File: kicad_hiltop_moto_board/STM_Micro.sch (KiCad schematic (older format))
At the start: 19 parts, among them SW1 SW_Push, U22 STM32F072RBTx, Y2 8MHZ, Y3 ABS25-32.768KHZ-6-T

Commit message: Unused pind removed from moto board
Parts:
- C73, C74, C75, C76, C77, C78, C79, C80, C81, C82: symbol Motor_Control_Board-rescue:C-device-Sensi_Board-rescue -> moto_board-rescue:C-device-Sensi_Board-rescue-Motor_Control_Board-rescue
- D13: symbol Motor_Control_Board-rescue:LED-device-Sensi_Board-rescue -> moto_board-rescue:LED-device-Sensi_Board-rescue-Motor_Control_Board-rescue
- L11: symbol Motor_Control_Board-rescue:Ferrite_Bead-device-Sensi_Board-rescue -> moto_board-rescue:Ferrite_Bead-device-Sensi_Board-rescue-Motor_Control_Board-rescue
- R120, R124: symbol Motor_Control_Board-rescue:R-device-Sensi_Board-rescue -> moto_board-rescue:R-device-Sensi_Board-rescue-Motor_Control_Board-rescue
- TP126: symbol Motor_Control_Board-rescue:Test_Point-Connector-Sensi_Board-rescue -> moto_board-rescue:Test_Point-Connector-Sensi_Board-rescue-Motor_Control_Board-rescue
- U22: symbol Motor_Control_Board-rescue:STM32F072RBTx-MCU_ST_STM32-Sensi_Board-rescue -> moto_board-rescue:STM32F072RBTx-MCU_ST_STM32-Sensi_Board-rescue-Motor_Control_Board-rescue
- Y2: symbol Motor_Control_Board-rescue:Crystal_GND24-device-Sensi_Board-rescue -> moto_board-rescue:Crystal_GND24-device-Sensi_Board-rescue-Motor_Control_Board-rescue
- Y3: symbol Motor_Control_Board-rescue:Crystal_GND23-device-Sensi_Board-rescue -> moto_board-rescue:Crystal_GND23-device-Sensi_Board-rescue-Motor_Control_Board-rescue
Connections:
- net labels added: STM_RES1, STM_RES2
- net labels removed: ADC1, ADC10, ADC11, ADC12, ADC13, ADC2, ADC3, ADC4, ADC5, ADC6, ADC7, ADC8, ADC9, GPIO10, GPIO11, GPIO12, GPIO13, GPIO14, GPIO15, GPIO16, GPIO17, GPIO18, GPIO19, GPIO9, STM_SCL, STM_SDA
- wire segments 131 -> 124
- no-connect marks 6 -> 30
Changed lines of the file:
@@
 EESchema Schematic File Version 4
-LIBS:Motor_Control_Board-cache
+LIBS:moto_board-cache
 EELAYER 30 0
 EELAYER END
@@
 $EndDescr
 $Comp
-L Motor_Control_Board-rescue:STM32F072RBTx-MCU_ST_STM32-Sensi_Board-rescue U22
+L moto_board-rescue:STM32F072RBTx-MCU_ST_STM32-Sensi_Board-rescue-Motor_Control_Board-rescue U22
 U 1 1 5F956EB6
 P 7400 4675
@@
 $EndComp
 $Comp
-L Motor_Control_Board-rescue:Ferrite_Bead-device-Sensi_Board-rescue L11
+L moto_board-rescue:Ferrite_Bead-device-Sensi_Board-rescue-Motor_Control_Board-rescue L11
 U 1 1 5F957109
 P 8225 2025
@@
 	8525 2025 8375 2025
 $Comp
-L Motor_Control_Board-rescue:C-device-Sensi_Board-rescue C82
+L moto_board-rescue:C-device-Sensi_Board-rescue-Motor_Control_Board-rescue C82
 U 1 1 5F957430
 P 7875 2250
@@
 $EndComp
 $Comp
-L Motor_Control_Board-rescue:C-device-Sensi_Board-rescue C73
+L moto_board-rescue:C-device-Sensi_Board-rescue-Motor_Control_Board-rescue C73
 U 1 1 5F957A1A
 P 2125 1625
@@
 $EndComp
 $Comp
-L Motor_Control_Board-rescue:C-device-Sensi_Board-rescue C74
+L moto_board-rescue:C-device-Sensi_Board-rescue-Motor_Control_Board-rescue C74
 U 1 1 5F957BC6
 P 2575 1625
@@
 $EndComp
 $Comp
-L Motor_Control_Board-rescue:C-device-Sensi_Board-rescue C79
+L moto_board-rescue:C-device-Sensi_Board-rescue-Motor_Control_Board-rescue C79
 U 1 1 5F957C44
 P 3025 1625
@@
 $EndComp
 $Comp
-L Motor_Control_Board-rescue:C-device-Sensi_Board-rescue C80
+L moto_board-rescue:C-device-Sensi_Board-rescue-Motor_Control_Board-rescue C80
 U 1 1 5F957C84
 P 3475 1625
@@
 	4400 3075 3825 3075
 $Comp
-L Motor_Control_Board-rescue:R-device-Sensi_Board-rescue R120
+L moto_board-rescue:R-device-Sensi_Board-rescue-Motor_Control_Board-rescue R120
 U 1 1 5F95CC59
 P 2725 2850
@@
 BOOT0
 $Comp
-L Motor_Control_Board-rescue:C-device-Sensi_Board-rescue C81
+L moto_board-rescue:C-device-Sensi_Board-rescue-Motor_Control_Board-rescue C81
 U 1 1 5F9616D2
 P 3825 3550
@@
 $EndComp
 $Comp
-L Motor_Control_Board-rescue:Crystal_GND23-device-Sensi_Board-rescue Y3
+L moto_board-rescue:Crystal_GND23-device-Sensi_Board-rescue-Motor_Control_Board-rescue Y3
 U 1 1 5F964614
 P 3225 6550
@@
 	3575 6525 4100 6525
 $Comp
-L Motor_Control_Board-rescue:C-device-Sensi_Board-rescue C77
+L moto_board-rescue:C-device-Sensi_Board-rescue-Motor_Control_Board-rescue C77
 U 1 1 5F96D367
 P 2850 6275
@@
 Connection ~ 3225 6275
 $Comp
-L Motor_Control_Board-rescue:C-device-Sensi_Board-rescue C78
+L moto_board-rescue:C-device-Sensi_Board-rescue-Motor_Control_Board-rescue C78
 U 1 1 5F96FC00
 P 2850 6825
@@
 Connection ~ 3225 6825
 $Comp
-L Motor_Control_Board-rescue:Crystal_GND24-device-Sensi_Board-rescue Y2
+L moto_board-rescue:Crystal_GND24-device-Sensi_Board-rescue-Motor_Control_Board-rescue Y2
 U 1 1 5F97410A
 P 3050 4325
@@
 	3050 4075 3050 4175
 $Comp
-L Motor_Control_Board-rescue:C-device-Sensi_Board-rescue C75
+L moto_board-rescue:C-device-Sensi_Board-rescue-Motor_Control_Board-rescue C75
 U 1 1 5F97DA85
 P 2825 4075
@@
 	2550 4075 2675 4075
 $Comp
-L Motor_Control_Board-rescue:C-device-Sensi_Board-rescue C76
+L moto_board-rescue:C-device-Sensi_Board-rescue-Motor_Control_Board-rescue C76
 U 1 1 5F97DA93
 P 2825 4625
@@
 	10400 4775 11800 4775
 Wire Wire Line
-	4400 4775 3925 4775
-Wire Wire Line
-	4400 4875 3925 4875
-Wire Wire Line
-	4400 5175 3925 5175
-Wire Wire Line
-	4400 5275 3925 5275
-Wire Wire Line
 	3225 6275 4000 6275
 Wire Wire Line
@@
 	10400 3675 11800 3675
 Wire Wire Line
-	4400 5075 3925 5075
-Wire Wire Line
 	10400 4575 11800 4575
 Wire Wire Line
@@
 	10400 5175 11800 5175
 Wire Wire Line
-	4400 4575 3925 4575
-Wire Wire Line
 	10400 6075 11775 6075
 Wire Wire Line
@@
 Wire Wire Line
 	10400 4275 11800 4275
-Wire Wire Line
-	4400 4975 3925 4975
 Wire Wire Line
 	10400 5675 11775 5675
@@
 Text HLabel 11775 5775 2    60   Output ~ 0
 DEBUG_UART_TX
-Text HLabel 11800 3375 2    60   Input ~ 0
-ADC3
-$Comp
-L Motor_Control_Board-rescue:R-device-Sensi_Board-rescue R124
+$Comp
+L moto_board-rescue:R-device-Sensi_Board-rescue-Motor_Control_Board-rescue R124
 U 1 1 5CB16726
 P 12600 3575
@@
 $EndComp
 $Comp
-L Motor_Control_Board-rescue:LED-device-Sensi_Board-rescue D13
+L moto_board-rescue:LED-device-Sensi_Board-rescue-Motor_Control_Board-rescue D13
 U 1 1 5CB1BE49
 P 13075 3575
@@
 Text HLabel 11800 3875 2    60   BiDi ~ 0
 GPIO2
-Text HLabel 11800 4775 2    60   BiDi ~ 0
-GPIO13
-Text HLabel 11775 5575 2    60   BiDi ~ 0
-GPIO10
 Text HLabel 11775 6075 2    60   BiDi ~ 0
 GPIO5
-Text HLabel 3925 4575 0    60   BiDi ~ 0
-GPIO9
-Text HLabel 4400 6075 0    60   BiDi ~ 0
-GPIO11
-Text HLabel 11800 4975 2    60   BiDi ~ 0
-GPIO14
 Text HLabel 11775 6275 2    60   BiDi ~ 0
 GPIO7
-Text HLabel 3925 5175 0    60   Input ~ 0
-ADC12
-Text HLabel 3925 5275 0    60   Input ~ 0
-ADC13
-Text HLabel 11800 3175 2    60   BiDi ~ 0
-GPIO12
 Text HLabel 3925 5575 0    60   BiDi ~ 0
 GPIO1
@@
 	3925 5475 4400 5475
 $Comp
-L Motor_Control_Board-rescue:Test_Point-Connector-Sensi_Board-rescue TP?
+L moto_board-rescue:Test_Point-Connector-Sensi_Board-rescue-Motor_Control_Board-rescue TP?
 U 1 1 62481FA3
 P 7100 1825
@@
 Text HLabel 11800 5275 2    60   Input ~ 0
 STM_SPI1_MOSI
-Text HLabel 11800 5375 2    60   Input ~ 0
-STM_SCL
-Text HLabel 11800 5475 2    60   Input ~ 0
-STM_SDA
 NoConn ~ 4400 5375
 NoConn ~ 4400 3475
@@
 Text HLabel 11800 4475 2    60   Input ~ 0
 SWD_SCK
-Text HLabel 3925 4875 0    60   Input ~ 0
-ADC9
-Text HLabel 3925 4775 0    60   Input ~ 0
-ADC8
-Text HLabel 11800 3475 2    60   Input ~ 0
-ADC4
-Text HLabel 11800 3275 2    60   Input ~ 0
-ADC2
-Text HLabel 11800 3075 2    60   Input ~ 0
-ADC1
 Text HLabel 4400 5675 0    60   BiDi ~ 0
 GPIO3
@@
 Wire Wire Line
 	10400 5975 11800 5975
-Text HLabel 3925 4975 0    60   Input ~ 0
-ADC10
-Text HLabel 3925 5075 0    60   Input ~ 0
-ADC11
 Wire Wire Line
 	7500 1725 7500 1825
-Text HLabel 11800 3675 2    60   Input ~ 0
-ADC5
-Text HLabel 11800 3775 2    60   Input ~ 0
-ADC6
-Text HLabel 11775 4875 2    60   Input ~ 0
-ADC7
 $Comp
 L power:PWR_FLAG #FLG0102
@@
 NoConn ~ 4400 5775
 NoConn ~ 4400 5875
-Text HLabel 4400 5975 0    60   BiDi ~ 0
-GPIO15
-Text HLabel 11800 4075 2    60   BiDi ~ 0
-GPIO16
-Text HLabel 11800 4575 2    60   BiDi ~ 0
-GPIO17
-Text HLabel 11775 5675 2    60   BiDi ~ 0
-GPIO18
-Text HLabel 11800 5975 2    60   BiDi ~ 0
-GPIO19
+NoConn ~ 4400 4575
+NoConn ~ 4400 4775
+NoConn ~ 4400 4875
+NoConn ~ 4400 4975
+NoConn ~ 4400 5075
+NoConn ~ 4400 5175
+NoConn ~ 4400 5275
+NoConn ~ 4400 5975
+NoConn ~ 4400 6075
+NoConn ~ 11800 3075
+NoConn ~ 11800 3175
+NoConn ~ 11800 3275
+NoConn ~ 11800 3375
+NoConn ~ 11800 3475
+NoConn ~ 11800 3675
+NoConn ~ 11800 3775
+NoConn ~ 11800 4075
+NoConn ~ 11800 4575
+NoConn ~ 11800 4875
+NoConn ~ 11800 5375
+NoConn ~ 11800 5475
+NoConn ~ 11775 5575
+NoConn ~ 11775 5675
+NoConn ~ 11800 5975
+Text HLabel 11800 4975 2    60   Input ~ 0
+STM_RES2
+Text HLabel 11800 4775 2    60   Input ~ 0
+STM_RES1
 $EndSCHEMATC

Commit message: Started on moto board layout
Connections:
- net GPIO1 renamed M_SCS
- net GPIO2 renamed M_AIN1
- net GPIO3 renamed M_AIN2
- net GPIO4 renamed M_BIN1
- net GPIO5 renamed M_BIN2
- net GPIO6 renamed M_SLEEPn
- net GPIO7 renamed M_RESET
- net GPIO8 renamed M_FAULTn
- net STM_SPI1_MISO renamed M_SDATO
- net STM_SPI1_MOSI renamed M_SDATI
- net STM_SPI1_SCK renamed M_SCLK
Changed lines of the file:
@@
 $Descr A3 16535 11693
 encoding utf-8
-Sheet 3 5
+Sheet 5 5
 Title ""
 Date "2019-10-01"
@@
 	13325 3575 13225 3575
 Text HLabel 11800 3975 2    60   BiDi ~ 0
-GPIO4
+M_BIN1
 Text HLabel 11800 4175 2    60   Output ~ 0
 USB_DATA_N
@@
 USB_DATA_P
 Text HLabel 11800 3875 2    60   BiDi ~ 0
-GPIO2
+M_AIN1
 Text HLabel 11775 6075 2    60   BiDi ~ 0
-GPIO5
+M_BIN2
 Text HLabel 11775 6275 2    60   BiDi ~ 0
-GPIO7
-Text HLabel 3925 5575 0    60   BiDi ~ 0
-GPIO1
+M_RESET
 Wire Wire Line
 	10400 5075 11800 5075
@@
 	10400 3175 11800 3175
 Text HLabel 3925 5475 0    60   BiDi ~ 0
-GPIO8
+M_FAULTn
 Wire Wire Line
 	2125 3275 4400 3275
 Text HLabel 11800 5075 2    60   Input ~ 0
-STM_SPI1_SCK
+M_SCLK
 Text HLabel 11800 5175 2    60   Input ~ 0
-STM_SPI1_MISO
+M_SDATO
 Text HLabel 11800 5275 2    60   Input ~ 0
-STM_SPI1_MOSI
+M_SDATI
 NoConn ~ 4400 5375
 NoConn ~ 4400 3475
@@
 SWD_SCK
 Text HLabel 4400 5675 0    60   BiDi ~ 0
-GPIO3
+M_AIN2
 Text HLabel 11775 6175 2    60   BiDi ~ 0
-GPIO6
+M_SLEEPn
 Text HLabel 11775 5875 2    60   Input ~ 0
 DEBUG_UART_RX
@@
 Text HLabel 11800 4775 2    60   Input ~ 0
 STM_RES1
+Text HLabel 3925 5575 0    60   BiDi ~ 0
+M_SCS
 $EndSCHEMATC

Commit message: Moto board awaiting review
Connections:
- net M_FAULTn: now also U22.53 (PC12/USART3_CK/USART4_CK); no longer U22.38 (PC7/TIM3_CH2)
- net M_RESET: now also U22.10 (PC2/ADC_IN12/I2S2_MCK/SPI2_MISO); no longer U22.36 (I2S2_SD/RTC_REFIN/SPI2_MOSI/SYS_WKUP7/TIM15_CH1N/TIM15_CH2/TIM1_CH3N/PB15)
- net M_SCS: now also U22.54 (PD2/TIM3_ETR/USART3_DE/USART3_RTS); no longer U22.39 (PC8/TIM3_CH3)
- net M_SLEEPn: now also U22.11 (PC3/ADC_IN13/I2S2_SD/SPI2_MOSI); no longer U22.35 (I2C2_SDA/I2S2_MCK/SPI2_MISO/TIM15_CH1/TIM1_CH2N/TSC_G6_IO4/USART3_DE/USART3_RTS/PB14)
- net PWM_1: now reaches U22.22 (ADC_IN6/COMP1_OUT/I2S1_MCK/SPI1_MISO/TIM16_CH1/TIM1_BKIN/TIM3_CH1/TSC_G2_IO3/USART3_CTS/PA6)
- net M_AIN1: no longer names the net of U22.41 (CRS_SYNC/RCC_MCO/TIM1_CH1/USART1_CK/PA8)
- net M_AIN2: no longer names the net of U22.40 (PC9/DAC_EXTI9/TIM3_CH4)
- net M_BIN1: no longer names the net of U22.42 (DAC_EXTI9/TIM15_BKIN/TIM1_CH2/TSC_G4_IO1/USART1_TX/PA9)
- net M_BIN2: no longer names the net of U22.34 (I2C2_SCL/I2S2_CK/SPI2_SCK/TIM1_CH1N/TSC_G6_IO3/USART3_CTS/PB13)
- new net PWM_2: U22.35 (I2C2_SDA/I2S2_MCK/SPI2_MISO/TIM15_CH1/TIM1_CH2N/TSC_G6_IO4/USART3_DE/USART3_RTS/PB14)
- no-connect marks 30 -> 32
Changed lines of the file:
@@
 P 3225 6550
 F 0 "Y3" V 3075 6400 50  0000 L CNN
-F 1 "ABS25-32.768KHZ-6-T" V 3375 6425 50  0000 L CNN
+F 1 "ABS25-32.768KHZ-6-T" V 3425 6375 50  0000 L CNN
 F 2 "Crystal:Crystal_SMD_7050-4Pin_7.0x5.0mm" H 3225 6550 50  0001 C CNN
 F 3 "" H 3225 6550 50  0001 C CNN
@@
 U 1 1 5F97410A
 P 3050 4325
-F 0 "Y2" V 2900 4175 50  0000 L CNN
+F 0 "Y2" V 2875 4225 50  0000 L CNN
 F 1 "8MHZ" V 3200 4350 50  0000 L CNN
 F 2 "Crystal:Crystal_SMD_Abracon_ABM3C-4Pin_5.0x3.2mm" H 3050 4325 50  0001 C CNN
@@
 U 1 1 5F97DA93
 P 2825 4625
-F 0 "C76" V 2600 4625 50  0000 C CNN
-F 1 "18pF" V 2675 4625 50  0000 C CNN
+F 0 "C76" V 2975 4625 50  0000 C CNN
+F 1 "18pF" V 3050 4650 50  0000 C CNN
 F 2 "Capacitor_SMD:C_0603_1608Metric" H 2863 4475 50  0001 C CNN
 F 3 "" H 2825 4625 50  0001 C CNN
@@
 Wire Wire Line
 	10400 6075 11775 6075
-Wire Wire Line
-	4400 5575 3925 5575
 Wire Wire Line
 	10400 5875 11775 5875
@@
 Wire Wire Line
 	13325 3575 13225 3575
-Text HLabel 11800 3975 2    60   BiDi ~ 0
-M_BIN1
 Text HLabel 11800 4175 2    60   Output ~ 0
 USB_DATA_N
 Text HLabel 11800 4275 2    60   Output ~ 0
 USB_DATA_P
-Text HLabel 11800 3875 2    60   BiDi ~ 0
-M_AIN1
-Text HLabel 11775 6075 2    60   BiDi ~ 0
-M_BIN2
-Text HLabel 11775 6275 2    60   BiDi ~ 0
+Text HLabel 4100 4975 0    60   BiDi ~ 0
 M_RESET
 Wire Wire Line
 	10400 5075 11800 5075
-Wire Wire Line
-	3925 5475 4400 5475
 $Comp
 L moto_board-rescue:Test_Point-Connector-Sensi_Board-rescue-Motor_Control_Board-rescue TP?
@@
 Wire Wire Line
 	10400 3175 11800 3175
-Text HLabel 3925 5475 0    60   BiDi ~ 0
+Text HLabel 4100 5975 0    60   BiDi ~ 0
 M_FAULTn
 Wire Wire Line
@@
 Text HLabel 11800 4475 2    60   Input ~ 0
 SWD_SCK
-Text HLabel 4400 5675 0    60   BiDi ~ 0
-M_AIN2
-Text HLabel 11775 6175 2    60   BiDi ~ 0
+Text HLabel 4100 5075 0    60   BiDi ~ 0
 M_SLEEPn
 Text HLabel 11775 5875 2    60   Input ~ 0
@@
 P 7750 1975
 F 0 "#FLG0102" H 7750 2050 50  0001 C CNN
-F 1 "PWR_FLAG" H 7750 2148 50  0000 C CNN
+F 1 "PWR_FLAG" H 7775 2175 50  0000 C CNN
 F 2 "" H 7750 1975 50  0001 C CNN
 F 3 "" H 7750 1975 50  0001 C CNN
@@
 P 3275 4325
 F 0 "#PWR0162" H 3275 4075 50  0001 C CNN
-F 1 "GND" H 3280 4152 50  0000 C CNN
+F 1 "GND" H 3400 4325 50  0000 C CNN
 F 2 "" H 3275 4325 50  0001 C CNN
 F 3 "" H 3275 4325 50  0001 C CNN
@@
 P 2800 4325
 F 0 "#PWR0165" H 2800 4075 50  0001 C CNN
-F 1 "GND" H 2805 4152 50  0000 C CNN
+F 1 "GND" H 2800 4200 50  0000 C CNN
 F 2 "" H 2800 4325 50  0001 C CNN
 F 3 "" H 2800 4325 50  0001 C CNN
@@
 NoConn ~ 4400 5775
 NoConn ~ 4400 5875
-NoConn ~ 4400 4575
-NoConn ~ 4400 4775
-NoConn ~ 4400 4875
-NoConn ~ 4400 4975
-NoConn ~ 4400 5075
 NoConn ~ 4400 5175
 NoConn ~ 4400 5275
-NoConn ~ 4400 5975
 NoConn ~ 4400 6075
 NoConn ~ 11800 3075
@@
 NoConn ~ 11800 3375
 NoConn ~ 11800 3475
-NoConn ~ 11800 3675
 NoConn ~ 11800 3775
 NoConn ~ 11800 4075
 NoConn ~ 11800 4575
 NoConn ~ 11800 4875
-NoConn ~ 11800 5375
-NoConn ~ 11800 5475
-NoConn ~ 11775 5575
-NoConn ~ 11775 5675
 NoConn ~ 11800 5975
 Text HLabel 11800 4975 2    60   Input ~ 0
@@
 Text HLabel 11800 4775 2    60   Input ~ 0
 STM_RES1
-Text HLabel 3925 5575 0    60   BiDi ~ 0
+Text HLabel 4100 4575 0    60   BiDi ~ 0
 M_SCS
+NoConn ~ 4400 5475
+NoConn ~ 4400 5575
+NoConn ~ 4400 5675
+NoConn ~ 11800 3875
+NoConn ~ 11800 3975
+NoConn ~ 11775 6075
+NoConn ~ 11775 6275
+NoConn ~ 11775 5575
+NoConn ~ 11775 5675
+NoConn ~ 4400 4775
+NoConn ~ 4400 4875
+Text HLabel 11800 3675 2    60   Output ~ 0
+PWM_1
+Text HLabel 11775 6175 2    60   Output ~ 0
+PWM_2
+NoConn ~ 11800 5475
+NoConn ~ 11800 5375
+Wire Wire Line
+	4400 4575 4100 4575
+Wire Wire Line
+	4400 4975 4100 4975
+Wire Wire Line
+	4400 5075 4100 5075
+Wire Wire Line
+	4400 5975 4100 5975
 $EndSCHEMATC

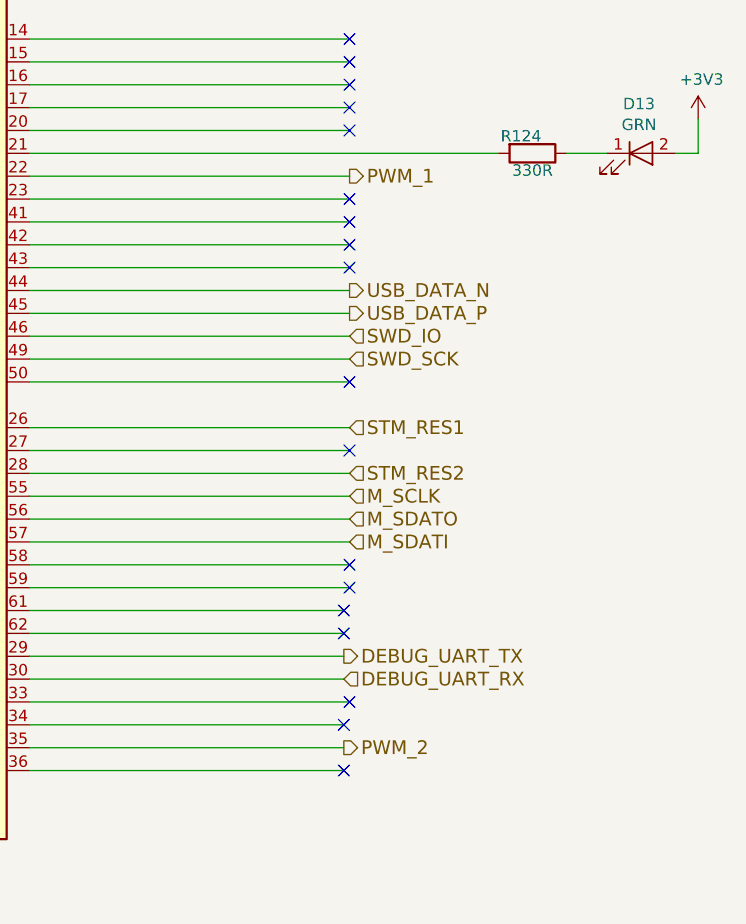
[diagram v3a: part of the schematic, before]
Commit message: Moto board connectors moved
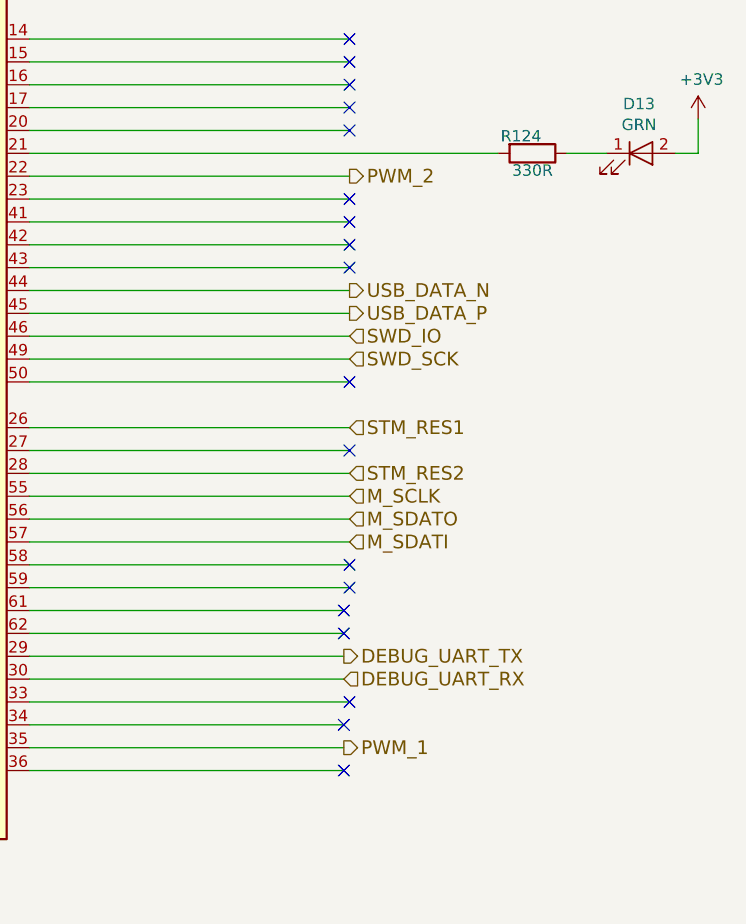
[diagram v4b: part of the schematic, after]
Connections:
- net PWM_1: now also U22.35 (I2C2_SDA/I2S2_MCK/SPI2_MISO/TIM15_CH1/TIM1_CH2N/TSC_G6_IO4/USART3_DE/USART3_RTS/PB14); no longer U22.22 (ADC_IN6/COMP1_OUT/I2S1_MCK/SPI1_MISO/TIM16_CH1/TIM1_BKIN/TIM3_CH1/TSC_G2_IO3/USART3_CTS/PA6)
- net PWM_2: now also U22.22 (ADC_IN6/COMP1_OUT/I2S1_MCK/SPI1_MISO/TIM16_CH1/TIM1_BKIN/TIM3_CH1/TSC_G2_IO3/USART3_CTS/PA6); no longer U22.35 (I2C2_SDA/I2S2_MCK/SPI2_MISO/TIM15_CH1/TIM1_CH2N/TSC_G6_IO4/USART3_DE/USART3_RTS/PB14)
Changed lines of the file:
@@
 NoConn ~ 4400 4775
 NoConn ~ 4400 4875
+Text HLabel 11775 6175 2    60   Output ~ 0
+PWM_1
 Text HLabel 11800 3675 2    60   Output ~ 0
-PWM_1
-Text HLabel 11775 6175 2    60   Output ~ 0
 PWM_2
 NoConn ~ 11800 5475
